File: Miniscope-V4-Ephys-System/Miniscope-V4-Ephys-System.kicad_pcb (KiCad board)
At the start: 6 copper layers, 67 parts, among them J1 34 Circuit Slimslack Connector, J10 Conn_01x01, J11 Conn_01x01, J12 Conn_01x01, J13 Conn_01x01, J14 Conn_01x05, J15 Conn_01x01, J16 Conn_01x01, J17 Conn_01x01, J18 Conn_01x01, J19 Conn_01x01, J2 Conn_01x01, J20 Conn_01x01, J21 Conn_01x01, J22 Conn_01x01, J23 Conn_01x01, J24 Conn_01x01, J25 Conn_01x01, J26 Conn_01x01, J27 Conn_01x01, J28 Conn_01x01, J3 Conn_01x01, J4 Conn_01x01, J5 Conn_01x01, J6 Conn_01x01, J7 Conn_01x01, J8 Conn_01x01, J9 Conn_01x01, Q1 MMBT3904LP-7B, U1 RHD2132, U2 TXB0304RUT, U3 MCP1711T-30I/5X, U4 ATSAME70N21A-CN, U5 MCP1711T-18I/5X, Y1 SMD_CRYSTAL

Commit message: Finish initial PCB layout.
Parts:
- J11, J13, J3, J5, J7, J9, U1, U4: moved to B.Cu
- moved C16 58.2 mm to (134.9, 117.7)
- moved C17 58.2 mm to (134.9, 116.2)
- moved Y1 58.2 mm to (132.4, 117.2)
- moved J21 55.5 mm to (128.5, 127.6), turned to 270 degrees
- moved J17 54.5 mm to (130.0, 127.6), turned to 270 degrees
- moved J18 54.3 mm to (127.0, 127.6), turned to 270 degrees
- moved J19 54.3 mm to (123.9, 127.6), turned to 270 degrees
- moved J11 54.0 mm to (128.4, 132.8), turned to 270 degrees
- moved J20 51.9 mm to (125.4, 127.6), turned to 270 degrees
- moved J3 48.7 mm to (129.9, 132.8), turned to 270 degrees
- moved J22 48.6 mm to (122.4, 127.6), turned to 270 degrees
- moved J13 48.3 mm to (122.1, 132.8), turned to 270 degrees
- moved J9 48.0 mm to (125.3, 132.8), turned to 270 degrees
- moved U4 47.2 mm to (126.2, 124.3), turned to 180 degrees
- moved J5 46.1 mm to (126.8, 132.8), turned to 270 degrees
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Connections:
- C16 pad 1: Net-(C16-Pad1) -> /MCU/XIN
- C17 pad 1: Net-(C17-Pad1) -> /MCU/XOUT
- Y1 pad 1: Net-(C16-Pad1) -> /MCU/XIN
- Y1 pad 3: Net-(C17-Pad1) -> /MCU/XOUT
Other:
- board outline added: 24 x 20.5 mm

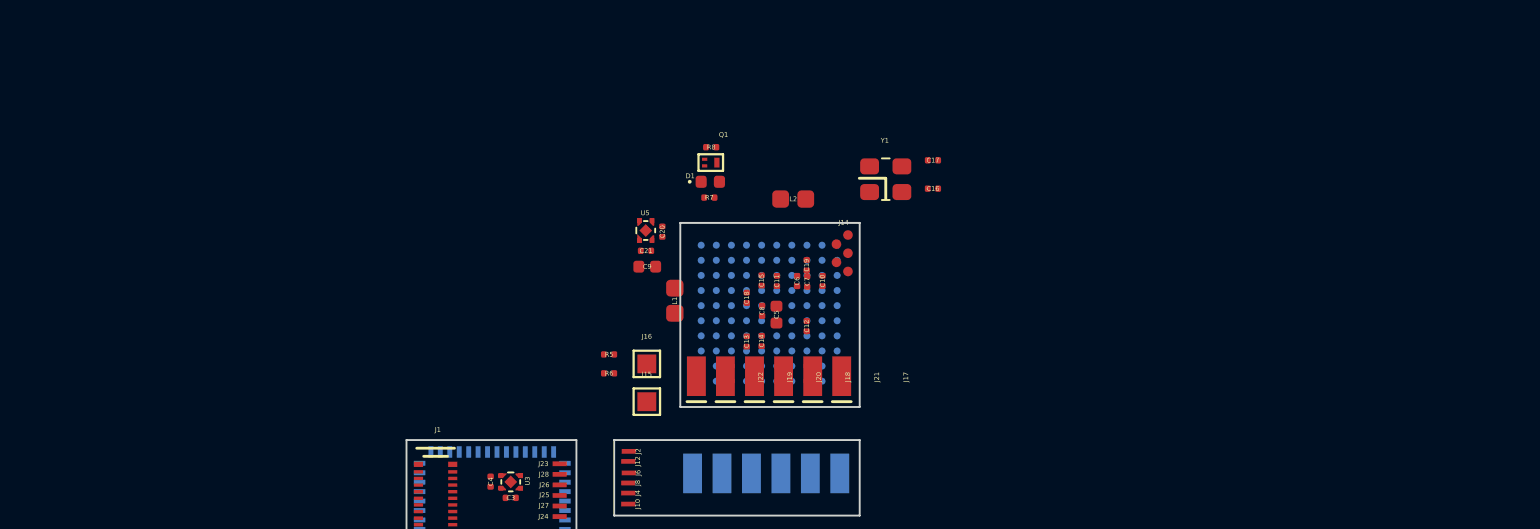
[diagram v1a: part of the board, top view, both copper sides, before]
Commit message: Finish layout of MCU PCB and routing of almost all traces.
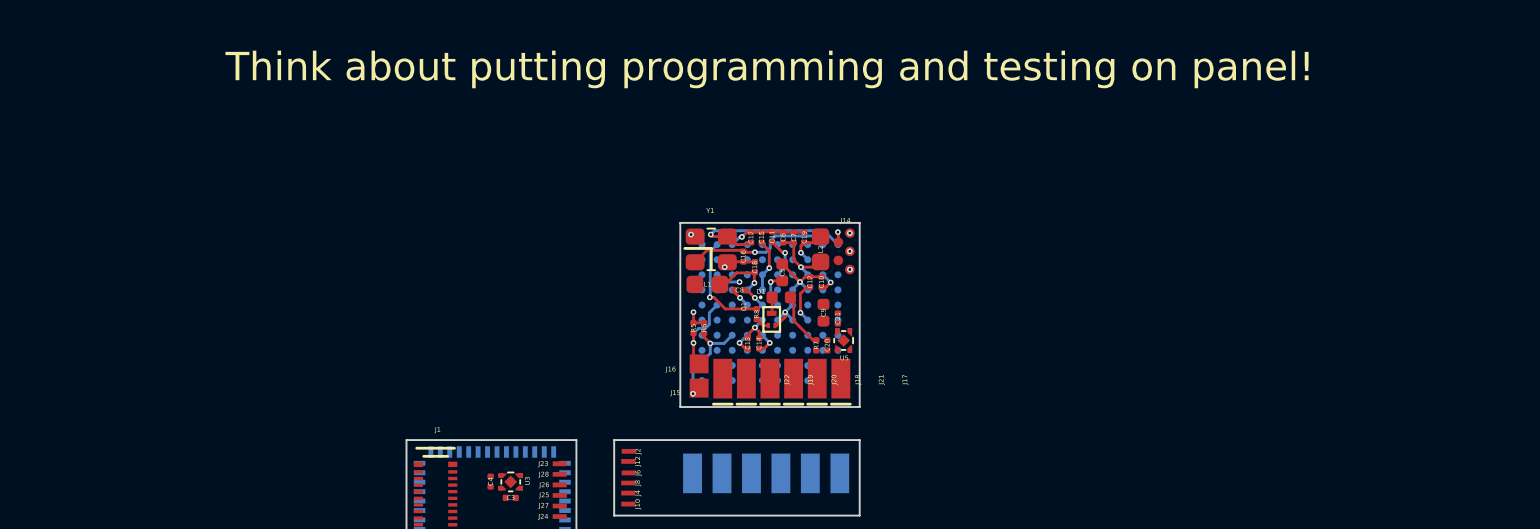
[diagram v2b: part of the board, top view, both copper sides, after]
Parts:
- J15, J16: footprint TestPoint:TestPoint_Pad_1.0x1.0mm -> .Connector:Conn_1x1_250x750_Pad
- moved U5 12.0 mm to (130.1, 125.7), turned to 180 degrees
- moved C21 10.8 mm to (129.8, 124.6), turned to 90 degrees
- moved C16 10.7 mm to (124.8, 121.3), turned to 270 degrees
- moved C20 10.6 mm to (129.3, 126.0), turned to 90 degrees
- moved C17 10.5 mm to (125.2, 120.3), turned to 90 degrees
- moved Y1 9.96 mm to (123.1, 120.9)
- moved R7 9.66 mm to (128.7, 126.0), turned to 90 degrees
- moved C9 9.65 mm to (129.1, 124.3), turned to 90 degrees
- moved R8 9.16 mm to (125.6, 124.3), turned to 90 degrees
- moved Q1 8.91 mm to (126.3, 124.6), turned to 90 degrees
- moved D1 7.18 mm to (126.8, 123.4)
- moved R6 5.57 mm to (122.8, 125.1), turned to 270 degrees
- moved R5 4.68 mm to (122.2, 125.1), turned to 270 degrees
- moved L2 3.04 mm to (128.9, 120.9), turned to 90 degrees
- moved J15 2.86 mm to (122.5, 128.2)
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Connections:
- net /MCU/SPI0_NPCS2 renamed Net-(U4-PadE10)
- net /MCU/SPI0_NPCS3 renamed Net-(U4-PadH4)
- C16 pad 1: /MCU/XIN -> /MCU/XOUT
- C17 pad 1: /MCU/XOUT -> /MCU/XIN
- U4 pad A7: /MCU/SPI0_NPCS1 -> Net-(U4-PadA7)
- U4 pad H3: /MCU/SPI0_NPCS1 -> Net-(U4-PadH3)
- Y1 pad 1: /MCU/XIN -> /MCU/XOUT
- Y1 pad 3: /MCU/XOUT -> /MCU/XIN
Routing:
- net GND: track 0.00 -> 16.2 mm, vias 0 -> 8
- net +1V8: track 0.00 -> 11.2 mm, vias 0 -> 7
- net /MCU/XIN: track 0.00 -> 9.94 mm, vias 0 -> 1
- net /MCU/XOUT: track 0.00 -> 7.84 mm, vias 0 -> 1
- net /MCU/VDDCORE: track 0.00 -> 7.81 mm, vias 0 -> 3
- net /MCU/SWDIO: track 0.00 -> 5.75 mm, vias 0 -> 2
- net /MCU/RED_LED: track 0.00 -> 5.70 mm, vias 0 -> 1
- net /MCU/SWDCLK: track 0.00 -> 4.40 mm, vias 0 -> 1
- net /MCU/VDDPLL: track 0.00 -> 3.22 mm, vias 0 -> 1
- net Net-(D1-Pad2): track 0.00 -> 2.93 mm
- net /MCU/VDDUTMIC: track 0.00 -> 2.12 mm, vias 0 -> 1
- net /MCU/TD: track 0.00 -> 1.36 mm, vias 0 -> 2
- net Net-(D1-Pad1): track 0.00 -> 0.85 mm
- net Net-(Q1-Pad1): track 0.00 -> 0.75 mm
- net /MCU/TF: track 0.00 -> 0.54 mm, vias 0 -> 1
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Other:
- net class Default: clearance 0.0762 -> 0.1016
- rule trace_clearance: 0.0762 -> 0.1016
- board text added: "Think about putting programming and testing on panel!"

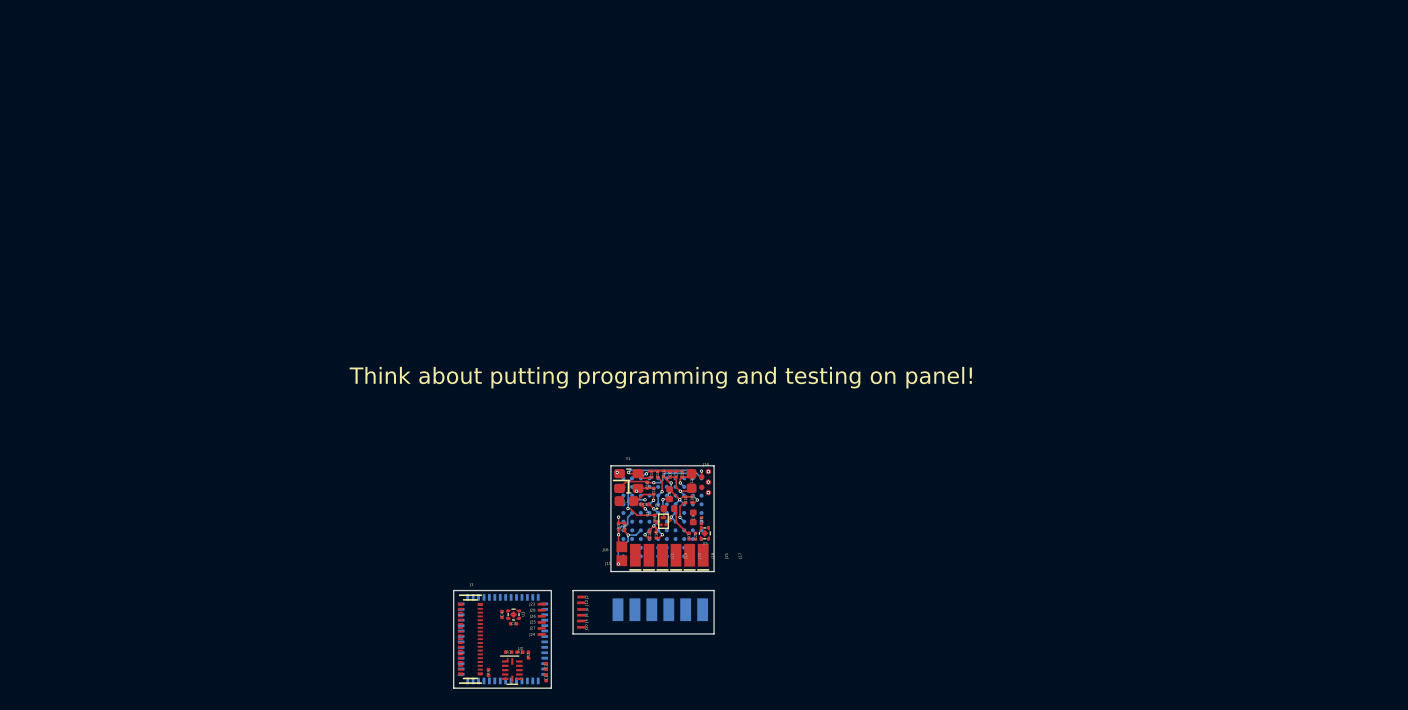
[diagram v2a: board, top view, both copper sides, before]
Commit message: Change orientation of some components and add notes to PCB layout
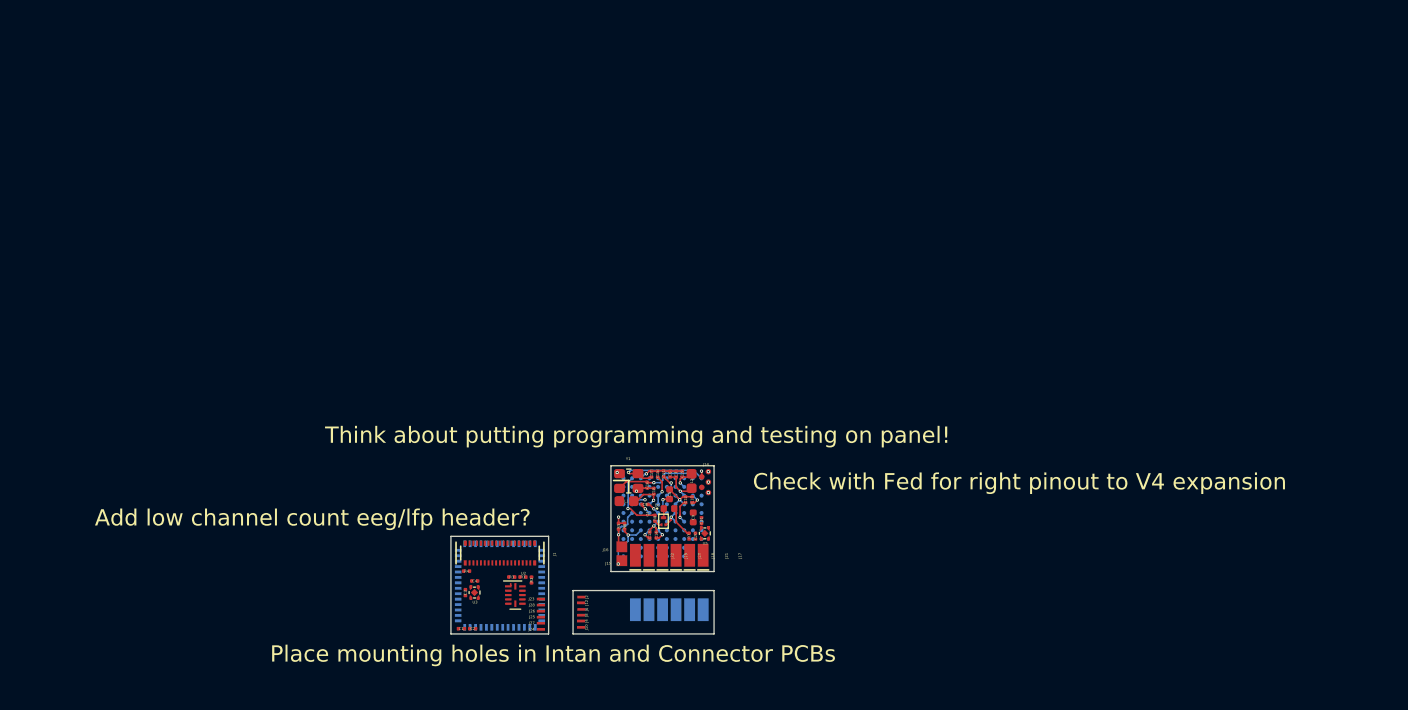
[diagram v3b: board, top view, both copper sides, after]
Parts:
- moved R4 9.56 mm to (108.2, 129.2), turned to 180 degrees
- moved C1 9.02 mm to (107.7, 134.5), turned to 180 degrees
- moved J1 8.39 mm to (111.3, 127.5), turned to 180 degrees
- moved C2 7.61 mm to (108.8, 134.5), turned to 180 degrees
- moved R1 6.93 mm to (113.4, 129.8)
- moved R2 6.93 mm to (114.2, 130.0)
- moved R3 6.93 mm to (112.3, 129.8)
- moved U2 6.93 mm to (112.7, 131.4)
- moved C3 5.29 mm to (108.1, 131.2), turned to 90 degrees
- moved U1 4.95 mm to (111.3, 130.5), turned to 270 degrees
- moved U3 4.13 mm to (108.9, 131.2), turned to 180 degrees
- moved C4 3.98 mm to (108.9, 130.1), turned to 180 degrees
- moved J13 1.60 mm to (123.8, 132.8)
- moved J7 1.29 mm to (125.0, 132.8)
- moved J9 0.98 mm to (126.2, 132.8)
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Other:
- board size 24 x 20.5 mm -> 24.2 x 15.5 mm
- board text added: "Add low channel count eeg/lfp header?"
- board text added: "Check with Fed for right pinout to V4 expansion"
- board text added: "Place mounting holes in Intan and Connector PCBs"

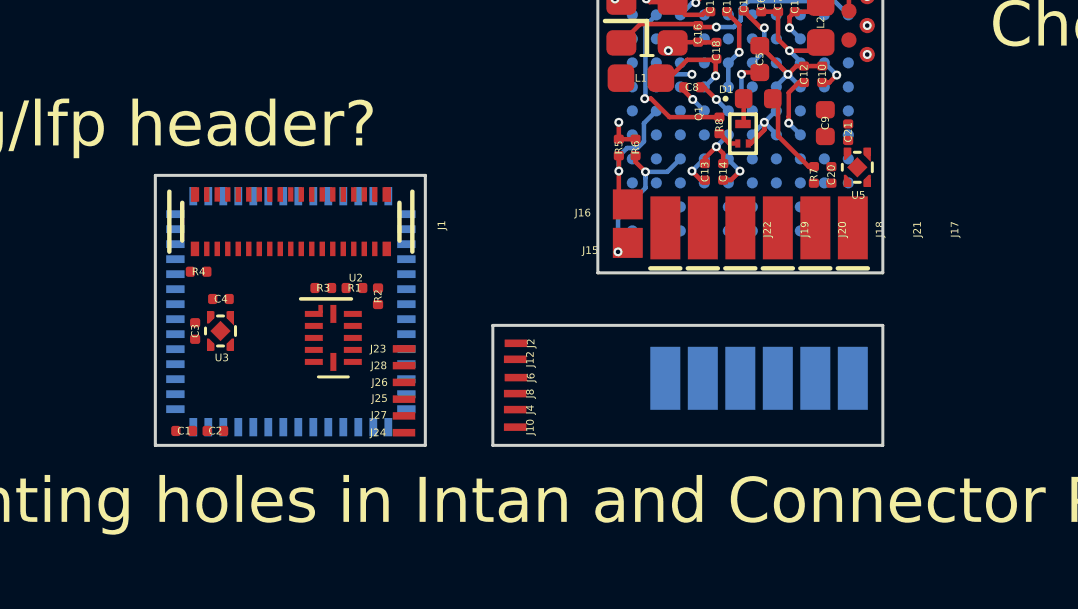
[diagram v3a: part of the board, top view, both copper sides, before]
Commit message: Switch to female slimstack and reorder pins to batch 32ch silicon probe connector
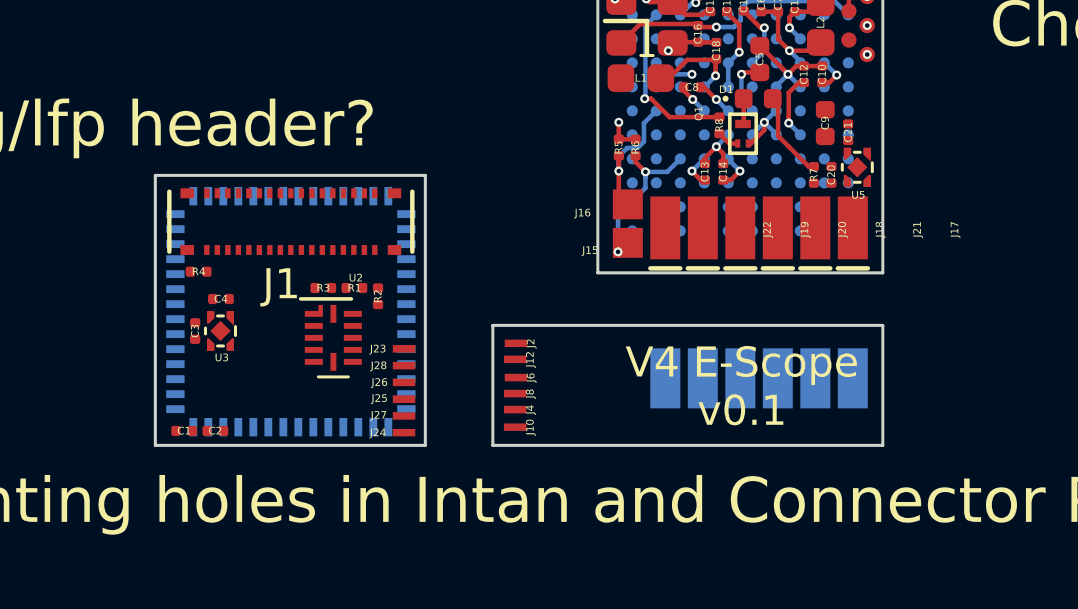
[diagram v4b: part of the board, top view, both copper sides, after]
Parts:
- J1: footprint .Connector:SS_5046223412 -> .Connector:SS_5046183412
- J11, J13, J3, J5, J7, J9: footprint .Connector:Spring_2306654_3 -> .Connector:Conn_1x1_250x750_Pad
- turned J11 to 0 degrees
- turned J13 to 0 degrees
- turned J3 to 0 degrees
- turned J5 to 0 degrees
- turned J7 to 0 degrees
- turned J9 to 0 degrees
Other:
- board text added: "V4 E-Scope v0.1"

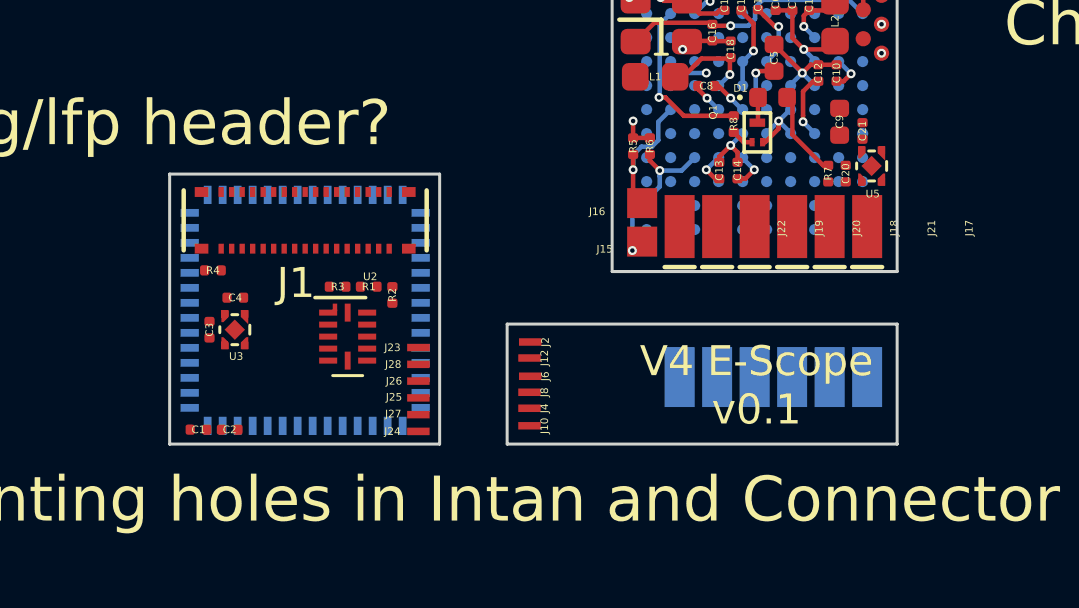
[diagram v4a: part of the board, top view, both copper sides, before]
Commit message: Finish routing Ephys and Connector PCBs. Decrease layer count to 4.
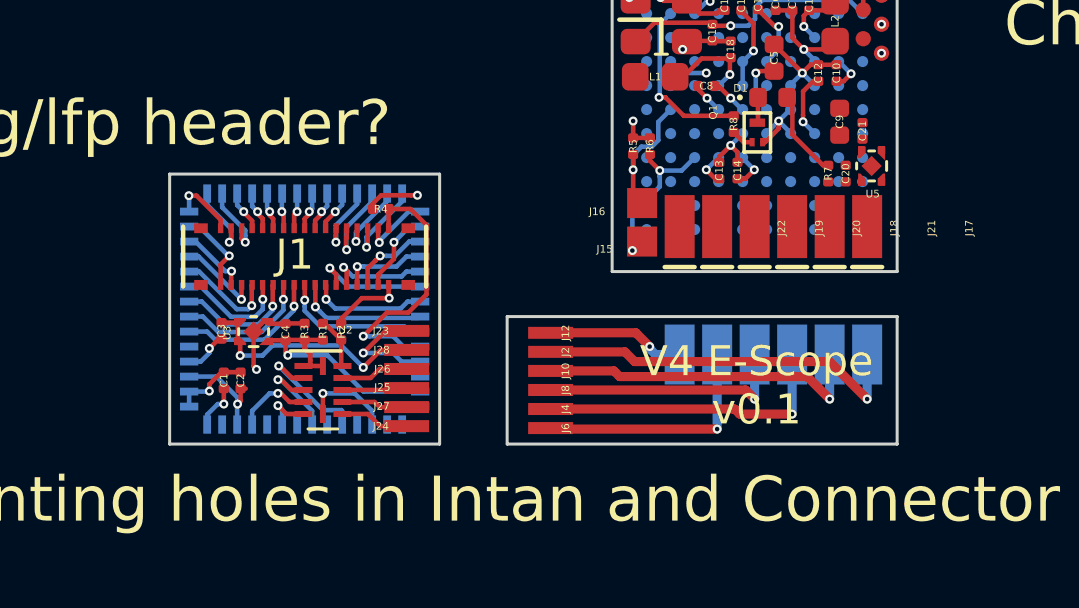
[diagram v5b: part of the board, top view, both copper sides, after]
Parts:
- moved R4 5.96 mm to (113.8, 127.2), turned to 0 degrees
- moved R1 2.14 mm to (111.9, 131.3), turned to 270 degrees
- moved R2 2.10 mm to (112.5, 131.3), turned to 270 degrees
- moved C4 2.03 mm to (110.6, 131.3), turned to 90 degrees
- moved U2 1.96 mm to (111.9, 133.2)
- moved J10 1.96 mm to (119.5, 132.6)
- moved R3 1.86 mm to (111.2, 131.3), turned to 270 degrees
- moved J6 1.86 mm to (119.5, 134.5)
- moved C1 1.85 mm to (108.6, 132.9), turned to 90 degrees
- moved C2 1.68 mm to (109.1, 132.9), turned to 90 degrees
- moved J1 1.21 mm to (111.2, 128.8)
- moved J12 1.10 mm to (119.5, 131.3)
- moved J2 0.76 mm to (119.5, 131.9)
- moved J11 0.75 mm to (128.8, 132.0)
- moved J13 0.75 mm to (123.8, 132.0)
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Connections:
- J1 pad 1: /Ephys/IN8 -> /Ephys/REF_ELEC
- J1 pad 10: /Ephys/IN17 -> /Ephys/IN16
- J1 pad 11: /Ephys/IN18 -> /Ephys/IN17
- J1 pad 12: /Ephys/IN19 -> /Ephys/IN18
- J1 pad 13: /Ephys/IN20 -> /Ephys/IN19
- J1 pad 14: /Ephys/IN21 -> /Ephys/IN20
- J1 pad 15: /Ephys/IN22 -> /Ephys/IN21
- J1 pad 16: /Ephys/IN23 -> /Ephys/IN22
- J1 pad 17: GND -> /Ephys/IN23
- J1 pad 18: /Ephys/REF_ELEC -> /Ephys/IN24
- J1 pad 19: /Ephys/IN24 -> /Ephys/IN25
- J1 pad 2: /Ephys/IN9 -> /Ephys/IN8
- J1 pad 20: /Ephys/IN25 -> /Ephys/IN26
- J1 pad 21: /Ephys/IN26 -> /Ephys/IN27
- J1 pad 22: /Ephys/IN27 -> /Ephys/IN28
- J1 pad 23: /Ephys/IN28 -> /Ephys/IN29
- J1 pad 24: /Ephys/IN29 -> /Ephys/IN30
- J1 pad 25: /Ephys/IN30 -> /Ephys/IN31
- J1 pad 26: /Ephys/IN31 -> /Ephys/IN0
- J1 pad 27: /Ephys/IN0 -> /Ephys/IN1
- J1 pad 28: /Ephys/IN1 -> /Ephys/IN2
- J1 pad 29: /Ephys/IN2 -> /Ephys/IN3
- J1 pad 3: /Ephys/IN10 -> /Ephys/IN9
- J1 pad 30: /Ephys/IN3 -> /Ephys/IN4
- J1 pad 31: /Ephys/IN4 -> /Ephys/IN5
- J1 pad 32: /Ephys/IN5 -> /Ephys/IN6
- J1 pad 33: /Ephys/IN6 -> /Ephys/IN7
- J1 pad 34: /Ephys/IN7 -> GND
- J1 pad 4: /Ephys/IN11 -> /Ephys/IN10
- J1 pad 5: /Ephys/IN12 -> /Ephys/IN11
- J1 pad 6: /Ephys/IN13 -> /Ephys/IN12
- J1 pad 7: /Ephys/IN14 -> /Ephys/IN13
- J1 pad 8: /Ephys/IN15 -> /Ephys/IN14
- J1 pad 9: /Ephys/IN16 -> /Ephys/IN15
- J23 pad 1: +5V -> GND
- J24 pad 1: /Ephys/CS_MCU -> /Ephys/MOSI_MCU
- J26 pad 1: /Ephys/MOSI_MCU -> /Ephys/CS_MCU
- J28 pad 1: GND -> +5V
- R4 pad 1: /Ephys/REF_ELEC -> GND
- R4 pad 2: GND -> /Ephys/REF_ELEC
- U2 pad 3: /Ephys/MOSI_RHD -> /Ephys/SCLK_RHD
- U2 pad 4: /Ephys/SCLK_RHD -> /Ephys/MISO_RHD
- U2 pad 5: /Ephys/MISO_RHD -> /Ephys/MOSI_RHD
- U2 pad 7: /Ephys/MISO_MCU -> /Ephys/MOSI_MCU
- U2 pad 8: /Ephys/SCLK_MCU -> /Ephys/MISO_MCU
- U2 pad 9: /Ephys/MOSI_MCU -> /Ephys/SCLK_MCU
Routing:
- net GND: track 16.2 -> 39.9 mm, vias 8 -> 16
- net +5V: track 0.00 -> 20.7 mm, vias 1 -> 4
- net +3V3: track 0.00 -> 12.7 mm, vias 0 -> 2
- net /Connector-Interface/CS_MCU: track 0.00 -> 11.2 mm, vias 0 -> 1
- net /Connector-Interface/MISO_MCU: track 0.00 -> 10.1 mm, vias 0 -> 1
- net /Ephys/REF_ELEC: track 0.00 -> 9.12 mm, vias 0 -> 1
- net /Connector-Interface/SPCK_MCU: track 0.00 -> 8.41 mm, vias 0 -> 1
- net /Connector-Interface/MOSI_MCU: track 0.00 -> 8.05 mm, vias 0 -> 1
- net /Ephys/IN0: track 0.00 -> 5.00 mm, vias 0 -> 1
- net /Ephys/IN31: track 0.00 -> 4.86 mm, vias 0 -> 1
- net /Ephys/IN30: track 0.00 -> 4.50 mm, vias 0 -> 1
- net /Ephys/IN1: track 0.00 -> 4.40 mm, vias 0 -> 1
- net /Ephys/CS_RHD: track 0.00 -> 4.18 mm, vias 0 -> 1
- net /Ephys/IN29: track 0.00 -> 4.14 mm, vias 0 -> 1
- net /Ephys/IN3: track 0.00 -> 3.91 mm, vias 0 -> 1
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- added copper zone on In2.Cu, net +3V3
- added copper zone on In1.Cu, net GND
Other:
- outline, holes or cut-outs redrawn
- copper layers 6 -> 4
